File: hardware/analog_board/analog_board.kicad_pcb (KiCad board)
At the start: 4 copper layers, 340 parts, among them J1 2x5 牛角座, J2 Conn_02x08_Counter_Clockwise, J3 Conn_01x04_Pin, J4 Conn_01x08, Q1 MMBT3906, Q2 MMBT3906, U1 GW2A-LV18EQ144, U10 TPS54360DDA, U11 TPS62933, U12 L7805, U13 L7905, U14 TPS7A4701xRGW, U15 TPS7A91, U16 L7815, U17 L7915, U19 AMS1117, U2 W25Q32JVSS, U3 AD9747BCPZ, U4 OPA695ID, U5 OPA695ID, U6 NE5532, U8 CDCI6214RGER, U9 TPS54360DDA, Y1 ASE-10MHz

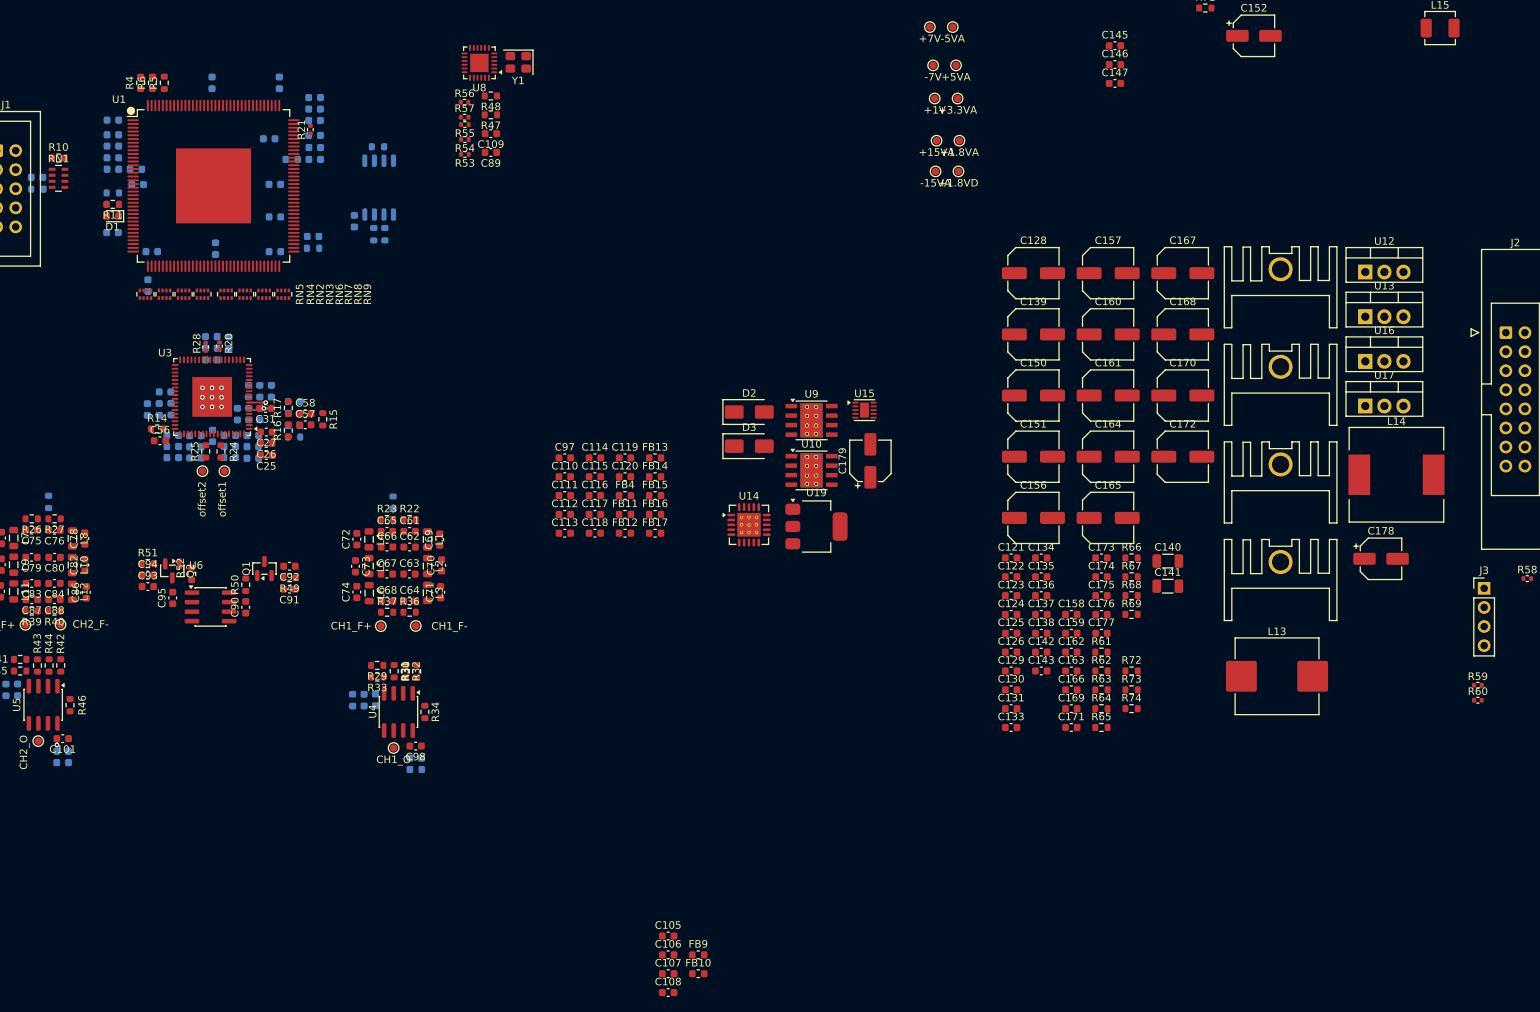
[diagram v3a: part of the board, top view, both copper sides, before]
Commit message: feat：时钟电路预布局
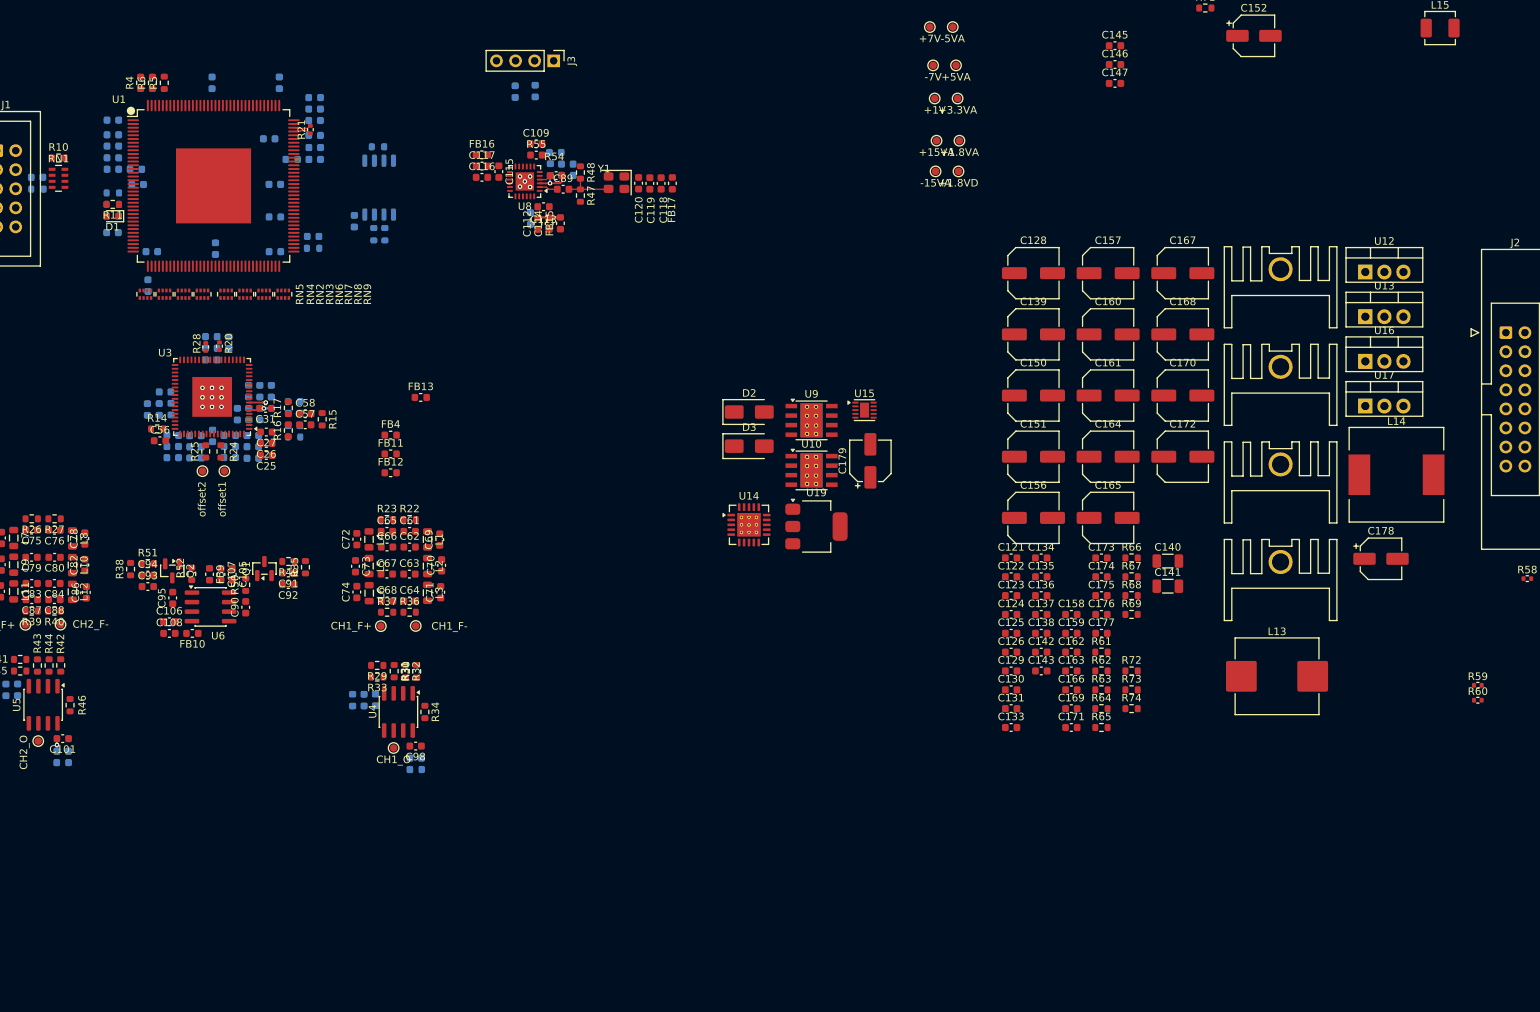
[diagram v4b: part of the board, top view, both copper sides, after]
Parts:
- C110, C111, C97, FB14: moved to B.Cu
- R35, R38: moved to F.Cu
- R53, R56, R57: footprint Resistor_SMD:R_0402_1005Metric -> Capacitor_SMD:C_0603_1608Metric; moved to B.Cu
- R54, R55: footprint Resistor_SMD:R_0402_1005Metric -> Capacitor_SMD:C_0603_1608Metric
- moved J3 142.5 mm to (153.5, 38.6), turned to -90 degrees
- moved FB9 82.5 mm to (107.7, 107.0), turned to -90 degrees
- moved C108 81.9 mm to (102.3, 114.9)
- moved FB10 81.2 mm to (105.4, 114.9), turned to 180 degrees
- moved C106 79.9 mm to (102.3, 113.3)
- moved C107 79.9 mm to (109.2, 107.0), turned to -90 degrees
- moved C105 75.5 mm to (110.7, 107.0), turned to -90 degrees
- moved FB16 53.2 mm to (143.9, 51.1)
- moved C117 48.8 mm to (144.0, 52.6)
- moved C118 47.4 mm to (167.8, 54.9), turned to -90 degrees
- moved FB17 46.7 mm to (169.3, 54.9), turned to -90 degrees
- moved FB14 45.2 mm to (153.7, 50.8)
- moved C116 45.0 mm to (144.0, 54.1)
- moved C113 43.6 mm to (152.2, 58.0), turned to 180 degrees
- moved C111 43.5 mm to (153.1, 53.1), turned to -90 degrees
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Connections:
- C57 pad 2: /DAC/DAC_CLK+ -> /Clock/DAC_CLK+
- C58 pad 2: /DAC/DAC_CLK+ -> /Clock/DAC_CLK+
- R15 pad 1: /DAC/DAC_CLK+ -> /Clock/DAC_CLK+
- R15 pad 2: /DAC/DAC_CLK+ -> /Clock/DAC_CLK+
- R21 pad 1: /FPGA/FPGA_CLK- -> /Clock/FPGA_CLK+
- R21 pad 2: /FPGA/FPGA_CLK+ -> /Clock/FPGA_CLK-
- U1 pad 105: /FPGA/FPGA_CLK- -> /Clock/FPGA_CLK+
- U1 pad 106: /FPGA/FPGA_CLK+ -> /Clock/FPGA_CLK-
- U8 pad 17: /FPGA/FPGA_CLK- -> /Clock/FPGA_CLK-
- U8 pad 18: /FPGA/FPGA_CLK+ -> /Clock/FPGA_CLK+
- U8 pad 21: /DAC/DAC_CLK+ -> /Clock/DAC_CLK-
- U8 pad 22: /DAC/DAC_CLK+ -> /Clock/DAC_CLK+
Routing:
- net /Clock/CLK_{IN}: track 0.00 -> 6.72 mm
- net Clock_V_{DD}: track 0.00 -> 5.30 mm, vias 0 -> 1
- net Clock_V_{VCO}: track 0.00 -> 3.02 mm
- net /Clock/XIN: track 0.00 -> 2.46 mm
- net /Clock/FPGA_CLK+: track 0.00 -> 2.39 mm
- net /Clock/FPGA_CLK-: track 0.00 -> 2.39 mm
- net Net-(U8-REFSEL): track 0.00 -> 1.62 mm
- net GND: vias 9 -> 14

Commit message: feat：模拟板电源预布局
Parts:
- removed C125, C126, C129, C130, C133, C134: 1uF, Capacitor_SMD:C_0603_1608Metric
- removed C150, C151, C156, C157: 100uF, Capacitor_SMD:C_Elec_6.3x7.7
- removed C158, C159: 100nF, Capacitor_SMD:C_0603_1608Metric
- removed HS1, HS3: Heatsink_Pad, Heatsink:TO-220_Heatsink
- removed TP12: +15VA, TestPoint:TestPoint_Pad_D1.0mm
- removed TP13: -15VA, TestPoint:TestPoint_Pad_D1.0mm
- removed U16: L7815, Package_TO_SOT_THT:TO-220-3_Vertical
- removed U17: L7915, Package_TO_SOT_THT:TO-220-3_Vertical
- added C144: 22uF, Capacitor_SMD:C_1206_3216Metric, F.Cu at (102.3, 124.1)
- added C180: 1uF, Capacitor_SMD:C_1206_3216Metric, F.Cu at (74.1, 150.0)
- added C181: 1uF, Capacitor_SMD:C_1206_3216Metric, F.Cu at (76.5, 150.0)
- added C182: 1uF, Capacitor_SMD:C_1206_3216Metric, F.Cu at (75.1, 119.3)
- added C183: 1uF, Capacitor_SMD:C_1206_3216Metric, F.Cu at (72.7, 119.3)
- added C184: 22uF, Capacitor_SMD:C_1206_3216Metric, F.Cu at (104.7, 124.1)
- added J5: CH1, Connector_Coaxial:SMA_BAT_Wireless_BWSMA-KWE-Z001, F.Cu at (160.7, 58.1)
- added J6: CH1, Connector_Coaxial:SMA_BAT_Wireless_BWSMA-KWE-Z001, F.Cu at (160.7, 77.0)
- C145, C146: footprint Capacitor_SMD:C_0603_1608Metric -> Capacitor_SMD:C_1206_3216Metric
- C166, C171: moved to B.Cu
- J2: footprint Connector_IDC:IDC-Header_2x08_P2.54mm_Latch_Vertical -> Connector_IDC:IDC_IDC-Header_2x08_P2.54mm_Vertical_antiClockWise
- moved J4 277.4 mm to (26.0, 151.1), turned to 90 degrees
- moved L15 249.8 mm to (45.7, 140.9)
- moved J2 249.1 mm to (31.7, 89.4), turned to 180 degrees
- moved R71 231.6 mm to (37.8, 143.9), turned to 90 degrees
- moved R70 231.5 mm to (39.3, 143.9), turned to -90 degrees
- moved U11 230.4 mm to (41.4, 143.8), turned to 90 degrees
- moved C152 228.6 mm to (47.5, 147.3), turned to -90 degrees
- moved C148 227.6 mm to (40.1, 140.9), turned to 90 degrees
- moved C154 227.3 mm to (53.1, 147.6), turned to 90 degrees
- moved C149 225.0 mm to (41.6, 140.9), turned to -90 degrees
- moved C153 224.8 mm to (51.2, 147.0), turned to 90 degrees
- moved C155 223.5 mm to (55.4, 147.6), turned to 90 degrees
- moved C145 216.7 mm to (42.3, 147.8), turned to 180 degrees
- moved C146 216.6 mm to (42.3, 150.1), turned to 180 degrees
- moved R59 215.4 mm to (64.8, 82.7), turned to 90 degrees
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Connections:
- C152 pad 2: -7V -> GND
- C153 pad 1: -7V -> GND
- C154 pad 1: -7V -> GND
- C155 pad 1: -7V -> GND
- HS4 pad 1: GND -> -7V
- J2 pad 1: /Ctrl_SPI_CS -> /FPGA_Ctrl.Ctrl_SPI_CS
- J2 pad 2: /Ctrl_SPI_CLK -> /FPGA_Ctrl.Ctrl_SPI_CLK
- J2 pad 3: /Ctrl_SPI_MISO -> /FPGA_Ctrl.Ctrl_SPI_MISO
- J2 pad 4: /Ctrl_SPI_MOSI -> /FPGA_Ctrl.Ctrl_SPI_MOSI
- J2 pad 6: /Ctrl_FPGA_NRST -> /FPGA_Ctrl.Ctrl_FPGA_NRST
- J2 pad 7: /GPIO1 -> /FPGA_Ctrl.GPIO1
- J2 pad 8: /GPIO2 -> /FPGA_Ctrl.GPIO2
- J4 pad 1: +3.3V -> +17V
- J4 pad 4: GND -> -17V
- J4 pad 5: +17V -> GND
- J4 pad 8: -17V -> +3.3V
- R58 pad 1: unconnected-(R58-Pad1) -> /DAC/DAC_SPI.DAC_SPI_MISO
- R58 pad 2: /DAC/DAC_SPI.DAC_SPI_MISO -> Net-(U3-SDO)
- R59 pad 1: unconnected-(R59-Pad1) -> /DAC/DAC_SPI.DAC_SPI_CLK
- R59 pad 2: /DAC/DAC_SPI.DAC_SPI_MOSI -> Net-(U1I-IOL42B)
- R60 pad 1: unconnected-(R60-Pad1) -> /DAC/DAC_SPI.DAC_SPI_MOSI
- R60 pad 2: /DAC/DAC_SPI.DAC_SPI_MISO -> Net-(U1I-IOL45A/LPLL2_T_in)
- U1 pad 124: /FPGA/GPIO2 -> /FPGA_Ctrl.GPIO2
- U1 pad 125: /FPGA/GPIO1 -> /FPGA_Ctrl.GPIO1
- U1 pad 126: /FPGA/Ctrl_FPGA_NRST -> /FPGA_Ctrl.Ctrl_FPGA_NRST
- U1 pad 129: /FPGA/Ctrl_SPI_MOSI -> /FPGA_Ctrl.Ctrl_SPI_MOSI
- U1 pad 130: /FPGA/Ctrl_SPI_MISO -> /FPGA_Ctrl.Ctrl_SPI_MISO
- U1 pad 131: /FPGA/Ctrl_SPI_CLK -> /FPGA_Ctrl.Ctrl_SPI_CLK
- U1 pad 132: /FPGA/Ctrl_SPI_CS -> /FPGA_Ctrl.Ctrl_SPI_CS
- U1 pad 33: /DAC/DAC_SPI.DAC_SPI_CLK -> Net-(U1I-IOL42B)
- U1 pad 34: /DAC/DAC_SPI.DAC_SPI_MOSI -> Net-(U1I-IOL45A/LPLL2_T_in)
- U3 pad 49: /DAC/DAC_SPI.DAC_SPI_MISO -> Net-(U3-SDO)
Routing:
- net Net-(U14-NR): track 0.00 -> 1.86 mm, vias 0 -> 1
- net GND: vias 14 -> 40

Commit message: feat：FPGA-DAC接口布线
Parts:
- FB13, FB4: moved to B.Cu
- moved C101 59.6 mm to (191.3, 89.5)
- moved C100 59.6 mm to (186.2, 49.4)
- moved C104 59.6 mm to (184.8, 97.1)
- moved C107 59.6 mm to (169.4, 68.4)
- moved C62 59.6 mm to (165.8, 43.3)
- moved C63 59.6 mm to (169.4, 43.3)
- moved C64 59.6 mm to (173.0, 43.3)
- moved C66 59.6 mm to (165.8, 46.3)
- moved C67 59.6 mm to (169.4, 46.3)
- moved C68 59.6 mm to (173.0, 46.3)
- moved C69 59.6 mm to (164.8, 39.3)
- moved C72 59.6 mm to (164.8, 50.3)
- moved C79 59.6 mm to (167.2, 93.7)
- moved C80 59.6 mm to (167.2, 90.6)
- moved C81 59.6 mm to (168.1, 97.7)
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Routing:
- net /DAC/P2D13: track 0.00 -> 25.5 mm
- net /DAC/P2D14: track 0.00 -> 25.4 mm
- net /DAC/P2D12: track 0.00 -> 25.4 mm
- net /DAC/P1D7: track 0.00 -> 25.4 mm
- net /DAC/P1D4: track 0.00 -> 25.4 mm
- net /DAC/P1D3: track 0.00 -> 25.3 mm
- net /DAC/P1D6: track 0.00 -> 25.3 mm
- net /DAC/P1D5: track 0.00 -> 25.3 mm
- net /DAC/P1D1: track 0.00 -> 25.3 mm
- net /DAC/P1D0: track 0.00 -> 25.2 mm
- net /DAC/P1D2: track 0.00 -> 25.2 mm
- net /DAC/P2D11: track 0.00 -> 25.2 mm
- net /DAC/P2D10: track 0.00 -> 25.2 mm
- net /DAC/P2D15: track 0.00 -> 25.2 mm
- net /DAC/P1D9: track 0.00 -> 25.2 mm
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
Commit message: feat：FPGA布线
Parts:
- added R75: 22R, Resistor_SMD:R_0402_1005Metric, F.Cu at (45.0, 71.2)
- C15, C18, C19, R13, R8: moved to F.Cu
- moved FB3 26.3 mm to (47.2, 82.3), turned to 0 degrees
- moved C10 24.8 mm to (47.2, 80.8), turned to 0 degrees
- moved C109 8.85 mm to (58.2, 29.8)
- moved R55 8.85 mm to (59.7, 29.8)
- moved C145 6.53 mm to (48.8, 147.8)
- moved C146 6.53 mm to (48.8, 150.1)
- moved C147 6.53 mm to (48.6, 145.9)
- moved C148 6.53 mm to (46.7, 140.9)
- moved C152 6.53 mm to (54.0, 147.3)
- moved C154 6.53 mm to (59.6, 147.6)
- moved C174 6.53 mm to (46.9, 126.8)
- moved C175 6.53 mm to (46.9, 125.2)
- moved J4 6.53 mm to (32.5, 151.1)
- moved R73 6.53 mm to (42.8, 125.3)
- moved R74 6.53 mm to (42.7, 126.9)
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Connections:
- U1 pad 130: /FPGA_Ctrl.Ctrl_SPI_MISO -> Net-(U1C-IOT17A)
- U14 pad 17: GND -> (no net)
- U14 pad 18: GND -> (no net)
- U14 pad 19: GND -> (no net)
- U14 pad 2: +3.3VA -> (no net)
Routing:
- net VCC_Core: track 0.00 -> 71.3 mm, vias 0 -> 4
- net /DAC/DAC_SPI.DAC_SPI_CS: track 0.00 -> 41.9 mm
- net +3.3V: track 0.00 -> 39.1 mm, vias 0 -> 14
- net /DAC/DAC_SPI.DAC_SPI_CLK: track 0.00 -> 37.9 mm
- net +1V0: track 0.00 -> 37.7 mm, vias 0 -> 3
- net /DAC/DAC_SPI.DAC_SPI_MOSI: track 0.00 -> 36.0 mm
- net /DAC/DAC_SPI.DAC_SPI_MISO: track 0.00 -> 34.5 mm
- net GND: track 6.22 -> 31.0 mm, vias 41 -> 71
- net VCC_PLLR: track 0.00 -> 16.5 mm, vias 0 -> 2
- net /FPGA_Ctrl.Ctrl_SPI_CS: track 0.00 -> 15.7 mm
- net /FPGA_Ctrl.GPIO2: track 0.00 -> 15.5 mm
- net /FPGA_Config/MSPI_MCLK: track 0.00 -> 15.2 mm, vias 0 -> 1
- net /FPGA_Config/MSPI_MO: track 0.00 -> 15.0 mm, vias 0 -> 1
- net /FPGA_Ctrl.Ctrl_SPI_CLK: track 0.00 -> 14.8 mm
- net /FPGA_Ctrl.GPIO1: track 0.00 -> 14.6 mm
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- added copper zone on In2.Cu, net +3.3V
- added copper zone on B.Cu, net GND
- added copper zone on In1.Cu, net GND
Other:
- board outline added: 212.3 x 151.4 mm

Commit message: feat：DAC布线
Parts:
- FB11, FB12: moved to B.Cu
- moved FB11 23.9 mm to (99.7, 69.5), turned to 0 degrees
- moved FB12 22.6 mm to (96.3, 66.4), turned to 0 degrees
- moved C35 6.18 mm to (103.8, 69.6)
- moved C32 6.12 mm to (88.1, 73.6), turned to 0 degrees
- moved C38 5.29 mm to (88.1, 72.1), turned to 0 degrees
- moved FB13 4.85 mm to (89.2, 67.8), turned to 180 degrees
- moved C42 4.47 mm to (102.0, 67.2)
- moved C34 4.47 mm to (91.9, 74.3), turned to 90 degrees
- moved C36 4.45 mm to (102.0, 64.2)
- moved C46 4.42 mm to (102.0, 71.8)
- moved C45 4.41 mm to (102.0, 74.9)
- moved C33 4.37 mm to (90.4, 74.3), turned to 90 degrees
- moved C50 3.24 mm to (86.9, 66.7), turned to -90 degrees
- moved C51 3.05 mm to (83.9, 66.7), turned to -90 degrees
- moved C28 2.39 mm to (95.9, 64.2), turned to 90 degrees
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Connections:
- C58 pad 2: /Clock/DAC_CLK+ -> /Clock/DAC_CLK-
- R15 pad 1: /Clock/DAC_CLK+ -> /Clock/DAC_CLK-
- U1 pad 30: unconnected-(U1I-IOL36B-Pad30) -> /DAC/DAC_SPI.DAC_RESET
- U3 pad 53: /DAC/DAC_RESET -> /DAC/DAC_SPI.DAC_RESET
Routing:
- net /DAC/DAC_SPI.DAC_RESET: track 0.00 -> 46.0 mm, vias 0 -> 2
- net +3.3VA_DAC: track 0.00 -> 40.2 mm, vias 0 -> 7
- net GND: track 31.0 -> 69.6 mm, vias 71 -> 78
- net +1.8VA_DAC: track 2.34 -> 22.8 mm, vias 1 -> 2
- net +1.8VD_DAC: track 8.18 -> 22.6 mm, vias 1 -> 3
- net +1.8VA: track 0.00 -> 10.00 mm, vias 0 -> 2
- net +3.3VD_DAC: track 0.00 -> 8.79 mm, vias 0 -> 1
- net Net-(C59-Pad2): track 0.00 -> 7.93 mm, vias 0 -> 2
- net /DAC/CLK-: track 0.00 -> 7.42 mm
- net /DAC/CLK+: track 0.00 -> 7.41 mm
- net /DAC/offset2: track 0.00 -> 6.14 mm
- net /DAC/offset1: track 0.00 -> 6.06 mm
- net +3.3VA: track 0.00 -> 3.23 mm, vias 0 -> 1
- net +3.3V: track 39.1 -> 41.4 mm, vias 14 -> 15
- net /DAC/REFIO: track 0.00 -> 2.17 mm
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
